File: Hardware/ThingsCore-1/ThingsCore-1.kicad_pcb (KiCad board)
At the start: 6 copper layers, 30 x 51 mm, 106 parts, among them IC1 WF200SD, Q1 Si2371EDS, Q2 Si2371EDS, Q3 2N7002, U2 K4B4G1646E-BYMA, U3 TLV62569DBV, U4 TLV62569DBV, U5 TLV62569DBV, U6 LAN8742A, U7 STM32MP133DAE7, U8 W25Q256JVEIQ, U9 TF-PUSH, Y1 X322516MLB4SI, Y2 Q13FC13500004

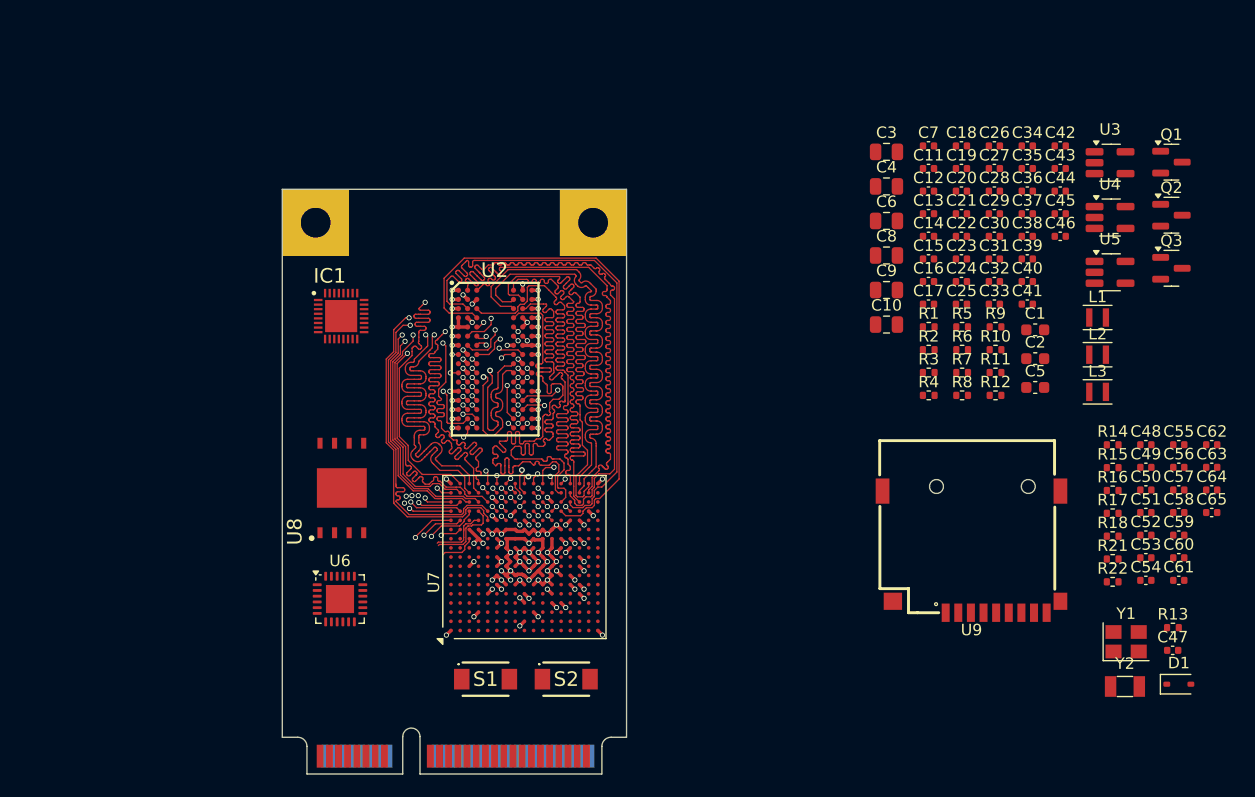
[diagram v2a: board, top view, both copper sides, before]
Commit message: layout transciever components, pin selection and last components
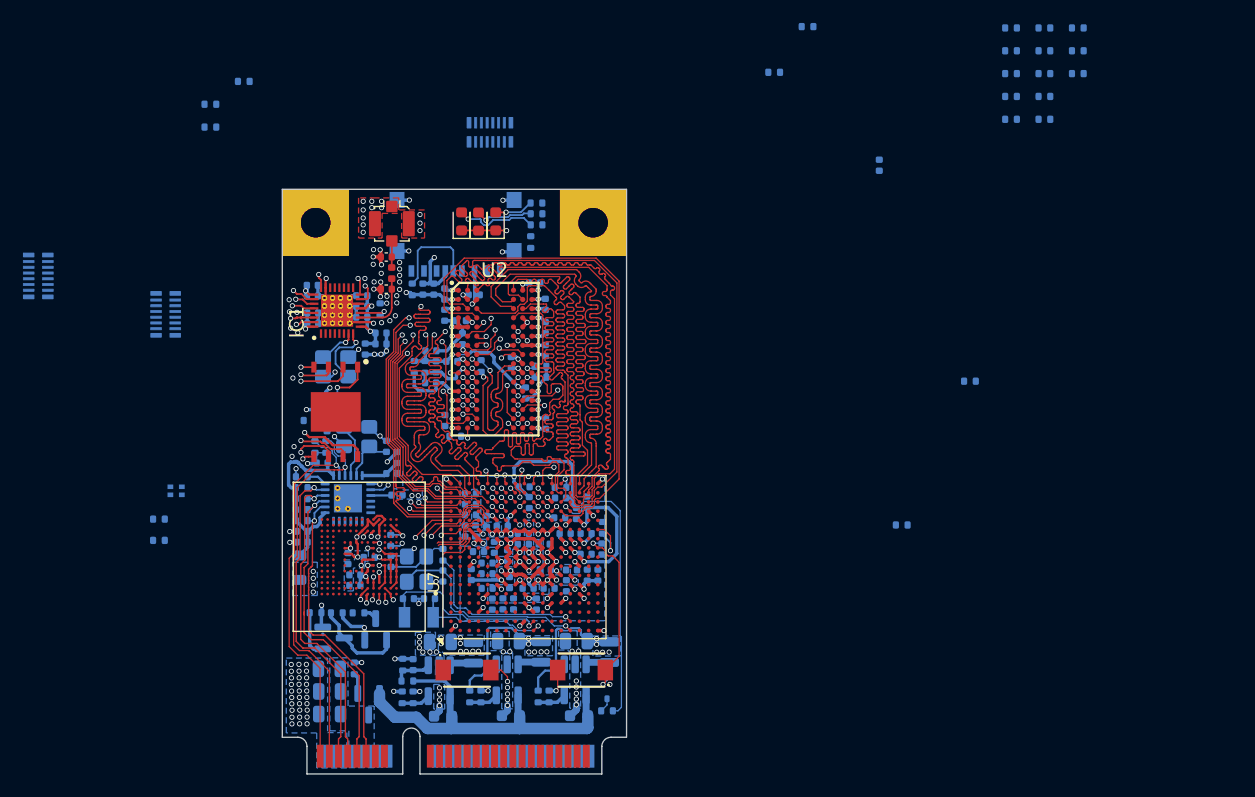
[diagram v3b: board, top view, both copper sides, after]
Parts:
- added C101: 100n, Capacitor_SMD:C_0402_1005Metric, B.Cu at (22.4, 39.0)
- added C66: 1u, Capacitor_SMD:C_0402_1005Metric, B.Cu at (38.9, 44.2)
- added C67: 10p, Capacitor_SMD:C_0402_1005Metric, B.Cu at (23.4, 48.1)
- added C68: 10p, Capacitor_SMD:C_0402_1005Metric, B.Cu at (25.2, 48.1)
- added C69: 15p, Capacitor_SMD:C_0402_1005Metric, B.Cu at (26.4, 46.1)
- added C70: 15p, Capacitor_SMD:C_0402_1005Metric, B.Cu at (21.9, 44.8)
- added C71: 100n, Capacitor_SMD:C_0402_1005Metric, B.Cu at (15.3, 31.1)
- added C72: 2.2u, Capacitor_SMD:C_0402_1005Metric, B.Cu at (16.2, 31.1)
- added C73: 2.2u, Capacitor_SMD:C_0402_1005Metric, B.Cu at (24.6, 21.1)
- added C74: 100n, Capacitor_SMD:C_0402_1005Metric, B.Cu at (25.6, 21.1)
- added C75: 2.2u, Capacitor_SMD:C_0402_1005Metric, B.Cu at (64.4, 10.3)
- added C76: 100n, Capacitor_SMD:C_0402_1005Metric, B.Cu at (20.0, 44.5)
- added C77: 2.2u, Capacitor_SMD:C_0402_1005Metric, B.Cu at (18.1, 44.6)
- added C78: 100n, Capacitor_SMD:C_0402_1005Metric, B.Cu at (18.7, 46.0)
- added C79: 100n, Capacitor_SMD:C_0402_1005Metric, B.Cu at (21.9, 43.0)
- added C80: 2.2u, Capacitor_SMD:C_0402_1005Metric, B.Cu at (18.7, 46.9)
- added C81: ~, Capacitor_SMD:C_0402_1005Metric, F.Cu at (21.5, 18.3)
- added C82: 2.2u, Capacitor_SMD:C_0402_1005Metric, F.Cu at (21.5, 21.1)
- added C83: 100n, Capacitor_SMD:C_0402_1005Metric, B.Cu at (15.1, 24.1)
- added C84: 10u, Capacitor_SMD:C_0402_1005Metric, B.Cu at (15.1, 23.2)
- added C85: 10u, Capacitor_SMD:C_0402_1005Metric, B.Cu at (15.0, 21.7)
- added C86: 10n, Capacitor_SMD:C_0402_1005Metric, B.Cu at (15.0, 20.8)
- added C87: 10u, Capacitor_SMD:C_0402_1005Metric, B.Cu at (19.3, 21.7)
- added C88: 33n, Capacitor_SMD:C_0402_1005Metric, B.Cu at (19.3, 22.6)
- added C89: 12p, Capacitor_SMD:C_0402_1005Metric, B.Cu at (19.3, 23.6)
- added C90: 12p, Capacitor_SMD:C_0402_1005Metric, B.Cu at (21.0, 24.9)
- added C91: 33n, Capacitor_SMD:C_0402_1005Metric, B.Cu at (21.0, 25.9)
- added C92: 10u, Capacitor_SMD:C_0402_1005Metric, B.Cu at (19.6, 26.3)
- added C93: 15p, Capacitor_SMD:C_0402_1005Metric, B.Cu at (21.5, 34.8)
- added C94: 15p, Capacitor_SMD:C_0402_1005Metric, B.Cu at (16.3, 33.0)
- added C95: 1u, Capacitor_SMD:C_0402_1005Metric, B.Cu at (22.4, 35.8)
- added C96: 470p, Capacitor_SMD:C_0402_1005Metric, B.Cu at (21.9, 37.2)
- added C97: 10u, Capacitor_SMD:C_0402_1005Metric, B.Cu at (14.1, 43.1)
- added C98: 100n, Capacitor_SMD:C_0402_1005Metric, B.Cu at (14.1, 42.2)
- added C99: 100n, Capacitor_SMD:C_0402_1005Metric, B.Cu at (15.9, 36.2)
- added D2: GREEN, LED_SMD:LED_0603_1608Metric, F.Cu at (28.0, 15.2)
- added D3: RED, LED_SMD:LED_0603_1608Metric, F.Cu at (29.5, 15.2)
- added D5: BLUE, LED_SMD:LED_0603_1608Metric, F.Cu at (31.0, 15.2)
- added FB1: 600Ω@100MHz, Inductor_SMD:L_0805_2012Metric, B.Cu at (13.9, 45.4)
- added J1: Conn_Coaxial, Connector_Coaxial:U.FL_Molex_MCRF_73412-0110_Vertical, F.Cu at (21.9, 15.4)
- added L4: ~, Inductor_SMD:L_0402_1005Metric, F.Cu at (21.9, 19.7)
- added R19: 1k, Resistor_SMD:R_0402_1005Metric, B.Cu at (18.7, 54.1)
- added R20: 33, Resistor_SMD:R_0402_1005Metric, B.Cu at (26.4, 44.2)
- added R23: 33, Resistor_SMD:R_0402_1005Metric, B.Cu at (14.8, 32.5)
- added R24: 10k, Resistor_SMD:R_0402_1005Metric, B.Cu at (17.1, 31.1)
- added R25: 33, Resistor_SMD:R_0402_1005Metric, B.Cu at (34.0, 17.0)
- added R26: 10k, Resistor_SMD:R_0402_1005Metric, B.Cu at (23.7, 21.1)
- added R27: 33, Resistor_SMD:R_0402_1005Metric, B.Cu at (6.13, 4.99)
- added R28: 10k, Resistor_SMD:R_0402_1005Metric, B.Cu at (6.13, 6.98)
- added R29: 0R, Resistor_SMD:R_0402_1005Metric, B.Cu at (9.04, 3.00)
- added R30: 10k, Resistor_SMD:R_0402_1005Metric, B.Cu at (1.65, 43.0)
- added R31: 10k, Resistor_SMD:R_0402_1005Metric, B.Cu at (1.65, 41.1)
- added R32: 1k, Resistor_SMD:R_0402_1005Metric, B.Cu at (34.5, 13.6)
- added R33: 1k, Resistor_SMD:R_0402_1005Metric, B.Cu at (34.6, 14.5)
- added R34: 1k, Resistor_SMD:R_0402_1005Metric, B.Cu at (34.6, 15.5)
- added R35: 3k, Resistor_SMD:R_0402_1005Metric, B.Cu at (40.3, 41.9)
- added R36: 10k, Resistor_SMD:R_0402_1005Metric, B.Cu at (72.3, 29.1)
- added R37: 50R, Resistor_SMD:R_0402_1005Metric, B.Cu at (20.9, 22.9)
- added R38: 0R, Resistor_SMD:R_0402_1005Metric, B.Cu at (55.3, 2.21)
- added R39: 12.1k, Resistor_SMD:R_0402_1005Metric, B.Cu at (14.1, 37.5)
- added R40: 10K, Resistor_SMD:R_0402_1005Metric, B.Cu at (16.2, 34.9)
- added R41: 10K, Resistor_SMD:R_0402_1005Metric, B.Cu at (15.2, 34.9)
- added R42: 0R, Resistor_SMD:R_0402_1005Metric, B.Cu at (58.2, -1.77)
- added R43: 49R9, Resistor_SMD:R_0402_1005Metric, B.Cu at (14.1, 39.4)
- added R44: 49R9, Resistor_SMD:R_0402_1005Metric, B.Cu at (14.1, 38.4)
- added R45: 49R9, Resistor_SMD:R_0402_1005Metric, B.Cu at (14.1, 41.3)
- added R46: 49R9, Resistor_SMD:R_0402_1005Metric, B.Cu at (14.1, 40.3)
- added R47: 33R, Resistor_SMD:R_0402_1005Metric, B.Cu at (75.9, -1.66)
- added R48: 33R, Resistor_SMD:R_0402_1005Metric, B.Cu at (75.9, 0.33)
- added R49: 33R, Resistor_SMD:R_0402_1005Metric, B.Cu at (75.9, 2.32)
- added R50: 33R, Resistor_SMD:R_0402_1005Metric, B.Cu at (75.9, 4.31)
- added R51: 33R, Resistor_SMD:R_0402_1005Metric, B.Cu at (75.9, 6.30)
- added R52: 33R, Resistor_SMD:R_0402_1005Metric, B.Cu at (78.8, -1.66)
- added R53: 10k, Resistor_SMD:R_0402_1005Metric, B.Cu at (78.8, 0.33)
- added R54: 10k, Resistor_SMD:R_0402_1005Metric, B.Cu at (78.8, 2.32)
- added R55: 33R, Resistor_SMD:R_0402_1005Metric, B.Cu at (78.8, 4.31)
- added R56: 33R, Resistor_SMD:R_0402_1005Metric, B.Cu at (78.8, 6.30)
- added R57: 33R, Resistor_SMD:R_0402_1005Metric, B.Cu at (81.7, -1.66)
- added R58: 33R, Resistor_SMD:R_0402_1005Metric, B.Cu at (81.7, 0.33)
- added R59: 33R, Resistor_SMD:R_0402_1005Metric, B.Cu at (81.7, 2.32)
- added RN1: R_Pack08_Split, ThingsCore-1:RESCAXS50P400X160X55-16N, B.Cu at (-8.87, 19.9)
- added RN2: R_Pack02_Split, Resistor_SMD:R_Array_Convex_2x0402, B.Cu at (3.15, 38.7)
- added RN3: R_Pack08_Split, ThingsCore-1:RESCAXS50P400X160X55-16N, B.Cu at (30.5, 7.43)
- added RN4: 22, ThingsCore-1:RESCAXS50P400X160X55-16N, B.Cu at (2.23, 23.3)
- added U10: EMMC04G-M627-A01, ThingsCore-1:BGA153C50P14X14_1300X1150X100, F.Cu at (19.1, 44.4)
- added Y3: C3SB38.400F09E12, Crystal:Crystal_SMD_3225-4Pin_3.2x2.5mm, B.Cu at (17.1, 27.9)
- added Y4: X322525MOB4SI, Crystal:Crystal_SMD_3225-4Pin_3.2x2.5mm, B.Cu at (18.9, 34.0)
- C1, C10, C11, C12, C13, C14, C15, C16, C17, C18, C19, C2, C20, C21, C22, C23, C24, C25, C26, C27, C28, C29, C3, C30, C31, C32, C33, C34, C35, C36, C37, C38, C39, C4, C40, C41, C42, C43, C44, C45, C46, C47, C48, C49, C5, C50, C51, C52, C53, C54, C55, C56, C57, C58, C59, C6, C60, C61, C62, C63, C64, C65, C7, C8, C9, D1, Q1, Q2, Q3, R1, R10, R11, R12, R13, R14, R15, R16, R17, R18, R2, R21, R22, R3, R4, R5, R6, R7, R8, R9, U3, U4, U5, U6, Y1, Y2: moved to B.Cu
- L1, L2, L3: footprint Inductor_SMD:L_Murata_DFE201610P -> ThingsCore-1:L_0805_2016; moved to B.Cu
- U9: value TF-PUSH -> TF-123B-ARP9H17; footprint ThingsCore-1:TF-PUSH -> ThingsCore-1:TF-SMD_TF-123-ARP9H15; moved to B.Cu
- moved Q1 84.4 mm to (19.9, 57.3), turned to -90 degrees
- moved Q3 79.8 mm to (16.9, 51.5)
- moved Q2 78.2 mm to (20.5, 50.8), turned to 90 degrees
- moved U3 73.9 mm to (26.1, 55.2), turned to -90 degrees
- moved C64 68.6 mm to (26.6, 23.4), turned to 90 degrees
- moved C65 67.3 mm to (26.6, 32.5), turned to 90 degrees
- moved C58 66.7 mm to (26.6, 21.5), turned to 90 degrees
- moved U4 66.2 mm to (32.0, 55.1), turned to -90 degrees
- moved C62 65.6 mm to (29.1, 21.6), turned to 180 degrees
- moved C52 64.3 mm to (25.4, 26.5), turned to 180 degrees
- moved C57 64.3 mm to (27.9, 23.9)
- moved C53 64.2 mm to (25.3, 29.3), turned to 180 degrees
- moved C7 63.7 mm to (23.8, 53.8), turned to -90 degrees
- moved R22 63.7 mm to (23.9, 27.9), turned to 90 degrees
- moved C54 63.2 mm to (28.1, 25.4), turned to -90 degrees
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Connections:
- net Net-(U3-EN) renamed /POWER/3V3_EN
- IC1 pad 10: unconnected-(IC1-GND_1-Pad10) -> GND
- IC1 pad 11: unconnected-(IC1-RF_1-Pad11) -> /NETWORKING/RF1
- IC1 pad 12: unconnected-(IC1-RF_2-Pad12) -> /NETWORKING/RF2
- IC1 pad 13: unconnected-(IC1-VDD_PA-Pad13) -> 3V3_VDD
- IC1 pad 14: unconnected-(IC1-RESERVE_1-Pad14) -> GND
- IC1 pad 15: unconnected-(IC1-RESETN-Pad15) -> /NETWORKING/TRX_~{RST}
- IC1 pad 16: unconnected-(IC1-GPIO/WUP-Pad16) -> /NETWORKING/TRX_WUP
- IC1 pad 23: unconnected-(IC1-GPIO/LP_CLK-Pad23) -> GND
- IC1 pad 24: unconnected-(IC1-GPIO/WIRQ-Pad24) -> /NETWORKING/TRX_IRQ
- IC1 pad 25: unconnected-(IC1-VDD_DIG-Pad25) -> 3V3_VDD
- IC1 pad 26: unconnected-(IC1-SDIO_CLK/_SPI_CLK-Pad26) -> /NETWORKING/TRX_CLK
- IC1 pad 27: unconnected-(IC1-SDIO_CMD/_SPI_MOSI-Pad27) -> /NETWORKING/TRX_CMD
- IC1 pad 28: unconnected-(IC1-SDIO_DAT0/_SPI_MISO-Pad28) -> /NETWORKING/TRX_D0
- IC1 pad 29: unconnected-(IC1-SDIO_DAT1_/_SPI_WIRQ-Pad29) -> /NETWORKING/TRX_D1
- IC1 pad 30: unconnected-(IC1-SDIO_DAT2/_HIF_SEL-Pad30) -> /NETWORKING/TRX_D2
- IC1 pad 31: unconnected-(IC1-SDIO_DAT3/_SPI_CSN-Pad31) -> /NETWORKING/TRX_D3
- IC1 pad 32: unconnected-(IC1-VDD_IO-Pad32) -> 3V3_VDD
- IC1 pad 33: unconnected-(IC1-GND_2-Pad33) -> GND
- IC1 pad 7: unconnected-(IC1-XTAL_I-Pad7) -> Net-(IC1-XTAL_I)
- IC1 pad 8: unconnected-(IC1-XTAL_O-Pad8) -> Net-(IC1-XTAL_O)
- IC1 pad 9: unconnected-(IC1-VDD_RF-Pad9) -> 3V3_VDD
- Q1 pad 1: GND -> Net-(Q1-G)
- Q2 pad 2: 3V3_VDD -> /POWER/VDD3V3_USBHS
- Q2 pad 3: /POWER/VDD3V3_USBHS -> 3V3_VDD
- S1 pad 1: unconnected-(S1-COM-Pad1) -> /MPU-IO/USER_SW
- S1 pad 2: unconnected-(S1-NO-Pad2) -> GND
- U1 pad 1: unconnected-(U1-Pad1) -> LED2
- U1 pad 10: unconnected-(U1-Pad10) -> VIN_EDGE
- U1 pad 11: unconnected-(U1-Pad11) -> TXN
- U1 pad 12: unconnected-(U1-Pad12) -> VIN_EDGE
- U1 pad 2: unconnected-(U1-Pad2) -> GND
- U1 pad 3: unconnected-(U1-Pad3) -> LED1
- U1 pad 4: unconnected-(U1-Pad4) -> GND
- U1 pad 5: unconnected-(U1-Pad5) -> RXP
- U1 pad 6: unconnected-(U1-Pad6) -> GND
- U1 pad 7: unconnected-(U1-Pad7) -> RXN
- U1 pad 8: unconnected-(U1-Pad8) -> VIN_EDGE
- U1 pad 9: unconnected-(U1-Pad9) -> TXP
- U6 pad 1: unconnected-(U6-VDD2A-Pad1) -> /NETWORKING/3V3_ETH_PHY
- U6 pad 10: unconnected-(U6-RXER/PHYAD0-Pad10) -> /NETWORKING/RXER
- U6 pad 11: unconnected-(U6-CRS_DV/MODE2-Pad11) -> /NETWORKING/CRS_DV
- U6 pad 12: unconnected-(U6-MDIO-Pad12) -> /NETWORKING/MDIO
- U6 pad 13: unconnected-(U6-MDC-Pad13) -> /NETWORKING/MDC
- U6 pad 14: unconnected-(U6-~{INT}/REFCLKO-Pad14) -> /NETWORKING/REFCLKO
- U6 pad 15: unconnected-(U6-~{RST}-Pad15) -> /NETWORKING/ETH_RST
- U6 pad 16: unconnected-(U6-TXEN-Pad16) -> /NETWORKING/TXEN
- U6 pad 17: unconnected-(U6-TXD0-Pad17) -> /NETWORKING/TXD0
- U6 pad 18: unconnected-(U6-TXD1-Pad18) -> /NETWORKING/TXD1
- U6 pad 19: unconnected-(U6-VDD1A-Pad19) -> /NETWORKING/3V3_ETH_PHY
- U6 pad 2: unconnected-(U6-LED2/~{INTSEL}-Pad2) -> LED2
- U6 pad 20: unconnected-(U6-TXN-Pad20) -> TXN
- U6 pad 21: unconnected-(U6-TXP-Pad21) -> TXP
- U6 pad 22: unconnected-(U6-RXN-Pad22) -> RXN
- U6 pad 23: unconnected-(U6-RXP-Pad23) -> RXP
- U6 pad 24: unconnected-(U6-RBIAS-Pad24) -> /NETWORKING/RBIAS
- U6 pad 25: unconnected-(U6-VSS-Pad25) -> GND
- U6 pad 3: unconnected-(U6-LED1/REGOFF-Pad3) -> LED1
- U6 pad 4: unconnected-(U6-XTAL2-Pad4) -> /NETWORKING/ETH_REF_OUT
- U6 pad 5: unconnected-(U6-XTAL1/CLKIN-Pad5) -> /NETWORKING/ETH_REF_IN
- U6 pad 6: unconnected-(U6-VDDCR-Pad6) -> /NETWORKING/VDDCR
- U6 pad 7: unconnected-(U6-RXD1/MODE1-Pad7) -> /NETWORKING/RXD1
- U6 pad 8: unconnected-(U6-RXD0/MODE0-Pad8) -> /NETWORKING/RXD0
- U6 pad 9: unconnected-(U6-VDDIO-Pad9) -> 3V3_VDD
- U7 pad K1: unconnected-(U7D-PC14-PadK1) -> /MPU-IO/LSE_IN
- U7 pad K2: unconnected-(U7D-PC15-PadK2) -> /MPU-IO/LSE_OUT
- U7 pad P1: unconnected-(U7E-PH0-PadP1) -> /MPU-IO/HSE_IN
- U7 pad P2: unconnected-(U7E-PH1-PadP2) -> /MPU-IO/HSE_OUT
- U7 pad U12: unconnected-(U7C-USB_RREF-PadU12) -> /MPU-IO/USB_RREF
- U8 pad 1: unconnected-(U8-~{CS}-Pad1) -> /MEMORY/QSPI1_~{CS}
- U8 pad 2: unconnected-(U8-DO/IO1-Pad2) -> /MEMORY/QSPI1_D1
- U8 pad 3: unconnected-(U8-~{WP}/IO2-Pad3) -> /MEMORY/QSPI1_D2
- U8 pad 4: unconnected-(U8-GND-Pad4) -> GND
- U8 pad 5: unconnected-(U8-DI/IO0-Pad5) -> /MEMORY/QSPI1_D0
- U8 pad 6: unconnected-(U8-CLK-Pad6) -> /MEMORY/QSPI1_CLK_NOR
- U8 pad 7: unconnected-(U8-~{HOLD}/~{RESET}/IO3-Pad7) -> /MEMORY/QSPI1_D3
- U8 pad 8: unconnected-(U8-VCC-Pad8) -> 3V3_VDD
- U9 pad 1: unconnected-(U9-DAT2-Pad1) -> /MEMORY/SD_D2
- U9 pad 10: unconnected-(U9-SHLD-Pad10) -> GND
- U9 pad 11: unconnected-(U9-SHLD-Pad11) -> GND
- U9 pad 12: unconnected-(U9-SHLD-Pad12) -> GND
- U9 pad 13: unconnected-(U9-SHLD-Pad13) -> GND
- U9 pad 2: unconnected-(U9-CS/DAT3-Pad2) -> /MEMORY/SD_D3
- U9 pad 3: unconnected-(U9-SDI/CMD-Pad3) -> /MEMORY/SD_CMD
- U9 pad 4: unconnected-(U9-VDD-Pad4) -> 3V3_VDD
- U9 pad 5: unconnected-(U9-CLK-Pad5) -> /MEMORY/SD_CLK_SD
- U9 pad 6: unconnected-(U9-VSS-Pad6) -> GND
- U9 pad 7: unconnected-(U9-SDO/DAT0-Pad7) -> /MEMORY/SD_D0
- U9 pad 8: unconnected-(U9-DAT1-Pad8) -> /MEMORY/SD_D1
- U9 pad 9: unconnected-(U9-CD-Pad9) -> /MEMORY/SD_DET
- Y1 pad 1: unconnected-(Y1-Pad1) -> /MPU-IO/HSE_IN
- Y1 pad 2: unconnected-(Y1-Pad2) -> GND
- Y1 pad 3: unconnected-(Y1-Pad3) -> /MPU-IO/HSE_OUT_C
- Y1 pad 4: unconnected-(Y1-Pad4) -> GND
- Y2 pad 1: unconnected-(Y2-Pad1) -> /MPU-IO/LSE_OUT
- Y2 pad 2: unconnected-(Y2-Pad2) -> /MPU-IO/LSE_IN
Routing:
- net GND: track 43.0 -> 146.9 mm, vias 54 -> 185
- net 3V3_VDD: track 14.8 -> 71.5 mm, vias 15 -> 40
- net 1V35_DDR: track 18.4 -> 56.9 mm, vias 23 -> 30
- net LED1: track 0.00 -> 34.3 mm, vias 0 -> 1
- net LED2: track 0.00 -> 34.1 mm, vias 0 -> 1
- net VIN: track 0.00 -> 32.9 mm
- net RXP: track 0.00 -> 28.2 mm, vias 0 -> 1
- net RXN: track 0.00 -> 27.7 mm, vias 0 -> 1
- net TXP: track 0.00 -> 27.0 mm, vias 0 -> 1
- net TXN: track 0.00 -> 25.9 mm, vias 0 -> 1
- net /MPU-IO/PWR_ON: track 0.57 -> 24.8 mm
- net /MPU-IO/HSE_IN: track 0.00 -> 18.4 mm, vias 0 -> 1
- net /NETWORKING/3V3_ETH_PHY: track 0.00 -> 16.9 mm
- net /MPU-IO/NRST: track 0.00 -> 16.0 mm, vias 0 -> 2
- net /MPU-IO/LSE_OUT: track 0.00 -> 15.8 mm, vias 0 -> 1
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- added copper zone on B.Cu, net 1V25_CORE
- added copper zone on B.Cu, net 1V35_DDR
- added copper zone on B.Cu, net 3V3_VDD
- added copper zone on B.Cu, net GND
- added copper zone on F.Cu, net GND
- added copper zone on B.Cu, net VIN_EDGE

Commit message: pin assignment, rst,led, button pins left and checks
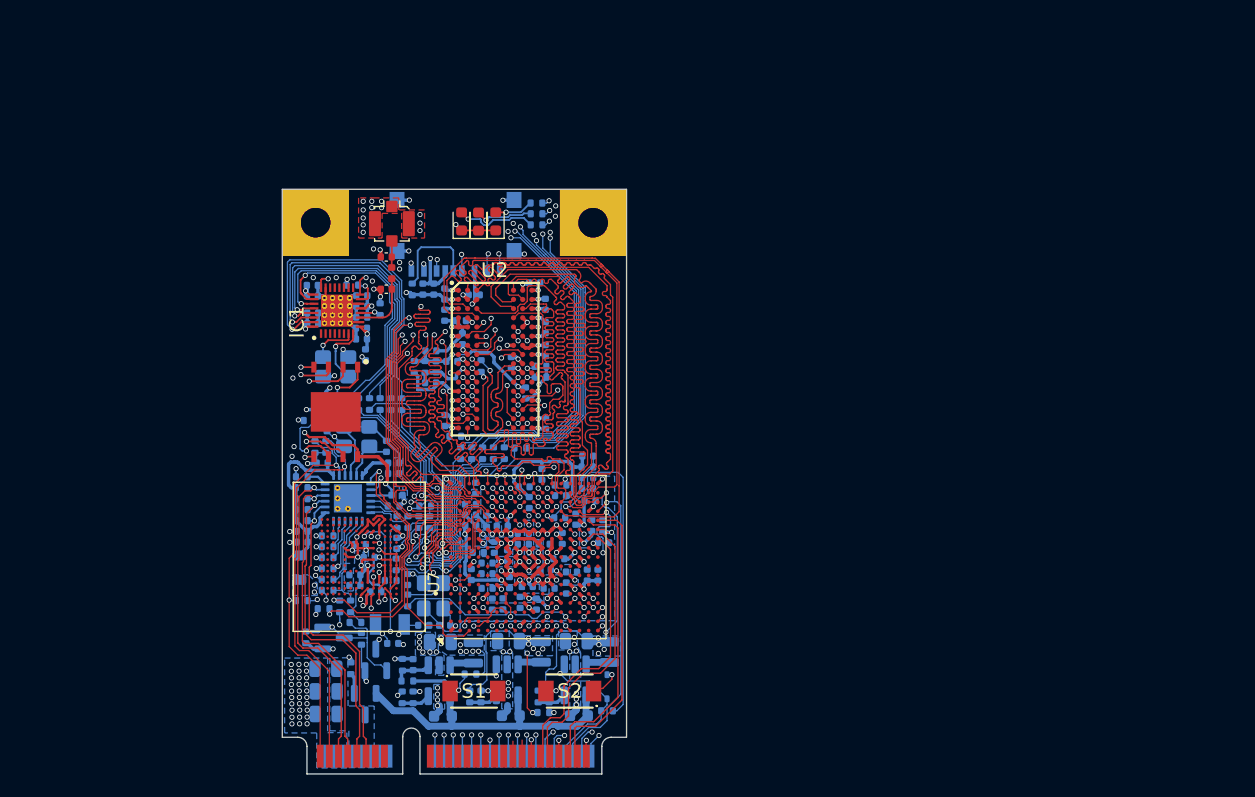
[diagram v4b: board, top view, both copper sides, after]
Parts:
- removed R29: 0R, Resistor_SMD:R_0402_1005Metric
- removed RN1, RN3: R_Pack08_Split, ThingsCore-1:RESCAXS50P400X160X55-16N
- removed RN2: R_Pack02_Split, Resistor_SMD:R_Array_Convex_2x0402
- removed RN4: 22, ThingsCore-1:RESCAXS50P400X160X55-16N
- added C100: 1u, Capacitor_SMD:C_0402_1005Metric, B.Cu at (39.0, 35.6)
- added C102: 1u, Capacitor_SMD:C_0402_1005Metric, B.Cu at (39.0, 38.5)
- added R60: 33R, Resistor_SMD:R_0402_1005Metric, B.Cu at (20.0, 31.1)
- added R61: 33R, Resistor_SMD:R_0402_1005Metric, B.Cu at (20.9, 31.1)
- added R62: 33R, Resistor_SMD:R_0402_1005Metric, B.Cu at (21.9, 31.1)
- added R63: 33R, Resistor_SMD:R_0402_1005Metric, B.Cu at (22.8, 31.1)
- added R64: 33R, Resistor_SMD:R_0402_1005Metric, B.Cu at (21.9, 46.5)
- added R65: 33R, Resistor_SMD:R_0402_1005Metric, B.Cu at (31.8, 35.4)
- added R66: 33R, Resistor_SMD:R_0402_1005Metric, B.Cu at (30.8, 35.4)
- added R67: 33R, Resistor_SMD:R_0402_1005Metric, B.Cu at (27.9, 35.4)
- added R68: 33R, Resistor_SMD:R_0402_1005Metric, B.Cu at (28.9, 35.4)
- added R69: 33R, Resistor_SMD:R_0402_1005Metric, B.Cu at (29.9, 35.4)
- added R70: 33R, Resistor_SMD:R_0402_1005Metric, B.Cu at (33.1, 35.0)
- added R71: 1k 1%, Resistor_SMD:R_0402_1005Metric, B.Cu at (39.0, 36.6)
- added R72: 1k 1%, Resistor_SMD:R_0402_1005Metric, B.Cu at (39.0, 37.5)
- R25, R27: value 33 -> 33R
- moved R58 79.8 mm to (18.4, 48.8), turned to -90 degrees
- moved R52 79.5 mm to (17.4, 48.8), turned to -90 degrees
- moved R47 76.5 mm to (16.4, 46.4)
- moved R54 75.9 mm to (16.4, 45.5)
- moved R56 74.7 mm to (16.4, 47.4)
- moved R48 73.6 mm to (16.4, 43.5)
- moved R51 73.5 mm to (16.0, 49.0)
- moved R57 72.5 mm to (23.4, 41.4), turned to -90 degrees
- moved R49 71.9 mm to (16.4, 42.6)
- moved R50 71.8 mm to (16.4, 44.5)
- moved R59 71.0 mm to (22.4, 41.4), turned to -90 degrees
- moved R53 69.2 mm to (22.1, 40.0), turned to 0 degrees
- moved R42 66.7 mm to (14.1, 48.2), turned to 0 degrees
- moved R55 65.9 mm to (24.3, 41.4), turned to -90 degrees
- moved C75 57.5 mm to (20.6, 47.5), turned to 180 degrees
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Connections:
- net /NETWORKING/NRST renamed TRX_~{RST}
- net /NETWORKING/TRX_IRQ renamed TRX_IRQ
- net /NETWORKING/TRX_WUP renamed TRX_WUP
- net /NETWORKING/TRX_~{RST} renamed /NETWORKING/TRX_RESETN
- C47 pad 2: /MPU-IO/NRST -> NRST
- C48 pad 2: /DDR3/DDR_VREF -> /DDR3/DDR_MPU_VREF
- D1 pad 1: /MPU-IO/NRST -> NRST
- D1 pad 2: /MPU-IO/PWR_ONRST -> PWR_ONRST
- R13 pad 1: /MPU-IO/PWR_ONRST -> PWR_ONRST
- R18 pad 1: GND -> /DDR3/ZQ
- R18 pad 2: /DDR3/ZQ -> GND
- R23 pad 1: /MEMORY/QSPI1_CLK -> QSPI1_CLK
- R24 pad 1: /MEMORY/QSPI1_~{CS} -> QSPI1_~{CS}
- R25 pad 1: /MEMORY/SD_CLK -> MMC1_CLK
- R25 pad 2: /MEMORY/SD_CLK_SD -> /NETWORKING/TRX_CLK
- R27 pad 1: /MEMORY/EMMC_CLK -> MMC1_CMD
- R27 pad 2: /MEMORY/EMMC_CLK_M6 -> /NETWORKING/TRX_CMD
- R28 pad 1: /MEMORY/EMMC_CMD -> MMC2_CMD
- R30 pad 1: /MEMORY/EMMC_D0 -> MMC2_D0
- R31 pad 1: /MEMORY/EMMC_CLK -> MMC2_CLK
- R42 pad 2: /NETWORKING/ETH_~{INT} -> ETH_~{INT}
- R47 pad 2: /NETWORKING/ETH_REF_CLK -> ETH_REF_CLK
- R48 pad 2: /NETWORKING/ETH_TX_D0 -> ETH_TX_D0
- R49 pad 2: /NETWORKING/ETH_TX_D1 -> ETH_TX_D1
- R50 pad 2: /NETWORKING/ETH_TX_EN -> ETH_TX_EN
- R51 pad 2: /NETWORKING/ETH_RX_D0 -> ETH_RX_D0
- R52 pad 2: /NETWORKING/ETH_RX_D0 -> ETH_RX_D1
- R55 pad 2: /NETWORKING/ETH_MDIO -> ETH_MDIO
- R56 pad 2: /NETWORKING/ETH_MDC -> ETH_MDC
- R59 pad 2: /NETWORKING/ETH_CRS_DV -> ETH_CRS_DV
- R9 pad 2: /POWER/VBAT -> VBAT
- S2 pad 1: /MPU-IO/NRST -> NRST
- U1 pad 18: unconnected-(U1-Pad18) -> /MPU-IO/ADC2_IN3
- U1 pad 20: unconnected-(U1-Pad20) -> /MPU-IO/ADC1_IN6
- U1 pad 22: unconnected-(U1-Pad22) -> /MPU-IO/ADC2_IN0
- U1 pad 24: unconnected-(U1-Pad24) -> /MPU-IO/ADC1_IN13
- U1 pad 26: unconnected-(U1-Pad26) -> /MPU-IO/ADC2_IN7
- U1 pad 28: unconnected-(U1-Pad28) -> /MPU-IO/ADC1_IN16
- U1 pad 30: unconnected-(U1-Pad30) -> GND
- U1 pad 32: unconnected-(U1-Pad32) -> VBAT
- U1 pad 34: unconnected-(U1-Pad34) -> DBG_JTCK
- U1 pad 36: unconnected-(U1-Pad36) -> DBG_JTDI
- U1 pad 38: unconnected-(U1-Pad38) -> DBG_JTDO
- U1 pad 39: unconnected-(U1-Pad39) -> GND
- U1 pad 40: unconnected-(U1-Pad40) -> DBG_JTMS
- U1 pad 41: unconnected-(U1-Pad41) -> /MPU-IO/USB2_N
- U1 pad 42: unconnected-(U1-Pad42) -> GND
- U1 pad 43: unconnected-(U1-Pad43) -> /MPU-IO/USB2_P
- U1 pad 44: unconnected-(U1-Pad44) -> NRST
- U1 pad 45: unconnected-(U1-Pad45) -> GND
- U1 pad 46: unconnected-(U1-Pad46) -> PWR_ONRST
- U1 pad 47: unconnected-(U1-Pad47) -> /MPU-IO/USB1_P
- U1 pad 48: unconnected-(U1-Pad48) -> BOOT0
- U1 pad 49: unconnected-(U1-Pad49) -> /MPU-IO/USB1_N
- U1 pad 50: unconnected-(U1-Pad50) -> BOOT1
- U1 pad 51: unconnected-(U1-Pad51) -> GND
- U1 pad 52: unconnected-(U1-Pad52) -> BOOT2
- U10 pad A3: /MEMORY/EMMC_D0 -> MMC2_D0
- U10 pad A4: /MEMORY/EMMC_D1 -> MMC2_D1
- U10 pad A5: /MEMORY/EMMC_D2 -> MMC2_D2
- U10 pad B2: /MEMORY/EMMC_D3 -> MMC2_D3
- U10 pad B3: /MEMORY/EMMC_D4 -> MMC2_D4
- U10 pad B4: /MEMORY/EMMC_D5 -> MMC2_D5
- U10 pad B5: /MEMORY/EMMC_D6 -> MMC2_D6
- U10 pad B6: /MEMORY/EMMC_D7 -> MMC2_D7
- U10 pad M5: /MEMORY/EMMC_CMD -> MMC2_CMD
- U10 pad M6: /MEMORY/EMMC_CLK_M6 -> /MEMORY/EMMC_CLK
- U4 pad 1: /POWER/PWR_ONRST -> PWR_ONRST
- U5 pad 1: /POWER/PWR_ONRST -> PWR_ONRST
- U7 pad A11: unconnected-(U7D-PC7-PadA11) -> MMC2_D7
- U7 pad A12: unconnected-(U7D-PB9-PadA12) -> MMC2_D5
- U7 pad A13: unconnected-(U7D-PB14-PadA13) -> MMC2_D0
- U7 pad A14: unconnected-(U7E-PG6-PadA14) -> MMC2_CMD
- U7 pad A15: unconnected-(U7D-PD2-PadA15) -> MMC1_CMD
- U7 pad A16: unconnected-(U7D-PC9-PadA16) -> MMC1_D1
- U7 pad A6: unconnected-(U7D-PD5-PadA6) -> QSPI1_D0
- U7 pad B11: unconnected-(U7D-PC6-PadB11) -> MMC2_D6
- U7 pad B12: unconnected-(U7D-PB15-PadB12) -> MMC2_D1
- U7 pad B13: unconnected-(U7D-PB4-PadB13) -> MMC2_D3
- U7 pad B14: unconnected-(U7D-PC10-PadB14) -> MMC1_D2
- U7 pad B15: unconnected-(U7D-PC12-PadB15) -> MMC1_CLK
- U7 pad B6: unconnected-(U7E-PE9-PadB6) -> QSPI1_D1
- U7 pad C1: unconnected-(U7D-PB6-PadC1) -> ETH_MDIO
- U7 pad C11: unconnected-(U7D-PB3-PadC11) -> MMC2_D2
- U7 pad C13: unconnected-(U7E-PF0-PadC13) -> MMC2_D4
- U7 pad C14: unconnected-(U7D-PC11-PadC14) -> MMC1_D3
- U7 pad C7: unconnected-(U7D-PD15-PadC7) -> QSPI1_D3
- U7 pad D13: unconnected-(U7E-PE3-PadD13) -> MMC2_CLK
- U7 pad D14: unconnected-(U7D-PC8-PadD14) -> MMC1_D0
- U7 pad D5: unconnected-(U7D-PD1-PadD5) -> QSPI1_~{CS}
- U7 pad E2: unconnected-(U7D-PD11-PadE2) -> QSPI1_D2
- U7 pad E3: unconnected-(U7D-PA12-PadE3) -> ETH_CRS_DV
- U7 pad F2: unconnected-(U7E-PG5-PadF2) -> ETH_MDC
- U7 pad G2: unconnected-(U7E-PF6-PadG2) -> ETH_TX_EN
- U7 pad G3: unconnected-(U7E-PF10-PadG3) -> QSPI1_CLK
- U7 pad G4: unconnected-(U7E-PG15-PadG4) -> ETH_~{INT}
- U7 pad G5: unconnected-(U7E-PF8-PadG5) -> ETH_~{INT}
- U7 pad H1: unconnected-(U7E-PH11-PadH1) -> ETH_REF_CLK
- U7 pad J2: /POWER/VBAT -> VBAT
- U7 pad L1: unconnected-(U7E-PE2-PadL1) -> ETH_RX_D1
- U7 pad L2: unconnected-(U7E-PF4-PadL2) -> ETH_RX_D0
- U7 pad M1: unconnected-(U7E-PF7-PadM1) -> ETH_TX_D0
- U7 pad M13: /DDR3/DDR_VREF -> /DDR3/DDR_MPU_VREF
- U7 pad M3: unconnected-(U7E-PG11-PadM3) -> ETH_TX_D1
- U7 pad P12: unconnected-(U7E-PI5-PadP12) -> BOOT1
- U7 pad P4: unconnected-(U7E-PF14-PadP4) -> DBG_JTCK
- U7 pad R10: unconnected-(U7E-PF15-PadR10) -> DBG_JTMS
- U7 pad R12: unconnected-(U7E-PI6-PadR12) -> BOOT2
- U7 pad R14: unconnected-(U7E-PH5-PadR14) -> DBG_JTDO
- U7 pad R4: unconnected-(U7D-PA1-PadR4) -> /MPU-IO/ADC2_IN3
- U7 pad T10: unconnected-(U7E-PDR_ON-PadT10) -> 3V3_VDD
- U7 pad T11: unconnected-(U7C-USB_DP2-PadT11) -> /MPU-IO/USB2_P
- U7 pad T13: unconnected-(U7C-USB_DP1-PadT13) -> /MPU-IO/USB1_P
- U7 pad T15: unconnected-(U7E-PH4-PadT15) -> DBG_JTDI
- U7 pad T3: unconnected-(U7D-PC0-PadT3) -> /MPU-IO/ADC2_IN0
- U7 pad T4: unconnected-(U7E-PF12-PadT4) -> /MPU-IO/ADC1_IN6
- U7 pad T5: unconnected-(U7D-PC3-PadT5) -> /MPU-IO/ADC1_IN13
- U7 pad U10: /MPU-IO/NRST -> NRST
- U7 pad U11: unconnected-(U7C-USB_DM2-PadU11) -> /MPU-IO/USB2_N
- U7 pad U13: unconnected-(U7C-USB_DM1-PadU13) -> /MPU-IO/USB1_N
- U7 pad U14: unconnected-(U7E-PI4-PadU14) -> BOOT0
- U7 pad U2: unconnected-(U7D-PA7-PadU2) -> /MPU-IO/ADC1_IN16
- U7 pad U3: unconnected-(U7D-PA0-PadU3) -> /MPU-IO/ADC2_IN7
- U8 pad 1: /MEMORY/QSPI1_~{CS} -> QSPI1_~{CS}
- U8 pad 2: /MEMORY/QSPI1_D1 -> QSPI1_D1
- U8 pad 3: /MEMORY/QSPI1_D2 -> QSPI1_D2
- U8 pad 5: /MEMORY/QSPI1_D0 -> QSPI1_D0
- U8 pad 7: /MEMORY/QSPI1_D3 -> QSPI1_D3
- U9 pad 5: /MEMORY/SD_CLK_SD -> /MEMORY/SD_CLK
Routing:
- net QSPI1_~{CS}: track 0.00 -> 48.0 mm, vias 0 -> 2
- net QSPI1_D2: track 0.00 -> 44.3 mm, vias 0 -> 2
- net QSPI1_CLK: track 0.00 -> 43.0 mm, vias 0 -> 2
- net ETH_TX_D1: track 0.00 -> 40.7 mm, vias 0 -> 2
- net /MEMORY/SD_D2: track 0.00 -> 39.7 mm, vias 0 -> 2
- net MMC2_D0: track 0.00 -> 39.6 mm, vias 0 -> 2
- net QSPI1_D1: track 0.00 -> 39.1 mm, vias 0 -> 2
- net /MEMORY/SD_D3: track 0.00 -> 38.8 mm, vias 0 -> 2
- net /MEMORY/SD_CMD: track 0.00 -> 38.5 mm, vias 0 -> 2
- net ETH_TX_EN: track 0.00 -> 38.4 mm, vias 0 -> 2
- net ETH_TX_D0: track 0.00 -> 36.4 mm, vias 0 -> 2
- net /MEMORY/SD_CLK: track 0.00 -> 35.6 mm, vias 0 -> 2
- net /POWER/VDDA1V8: track 5.79 -> 40.5 mm, vias 1 -> 2
- net /MEMORY/SD_D0: track 0.00 -> 33.9 mm, vias 0 -> 2
- net MMC2_CMD: track 0.00 -> 33.7 mm, vias 0 -> 3
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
